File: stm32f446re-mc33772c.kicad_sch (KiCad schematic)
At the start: 47 parts, among them J1 Conn_01x02, J2 USB_B_Micro, J3 Conn_01x03, J4 Conn_01x03, J6 SM06B-GHS-TB, U1 STM32F446RET6, U3 LD1086D2M33TR, U4 AMS1117-3.3, U6 LMR51450SDRRR, U7 SN65HVD232, Y1 16MHz

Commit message: fix: VCAP_1 4.7uF, In1.Cu fill GND
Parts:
- added C62: 4.7u, Capacitor_SMD:C_0402_1005Metric, symbol Device:C
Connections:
- net GND: now also C62.2
- net at U1.30 (VCAP_1): now also C62.1
- no-connect marks 39 -> 38

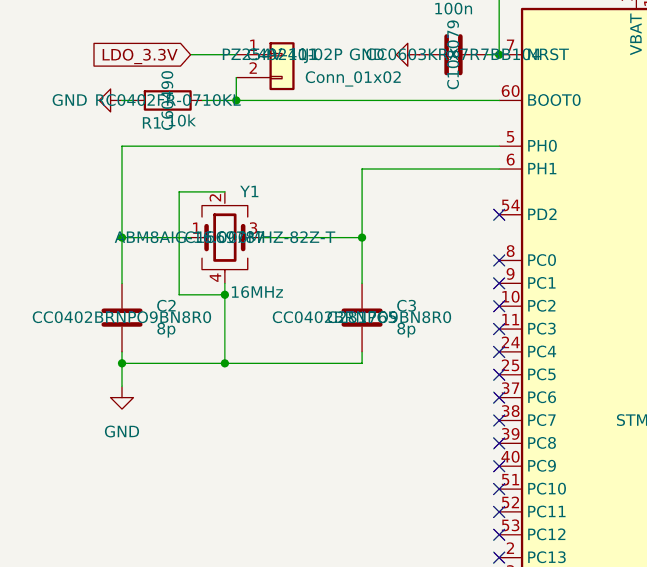
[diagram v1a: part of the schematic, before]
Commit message: change crystal from 16MHz to 8MHz
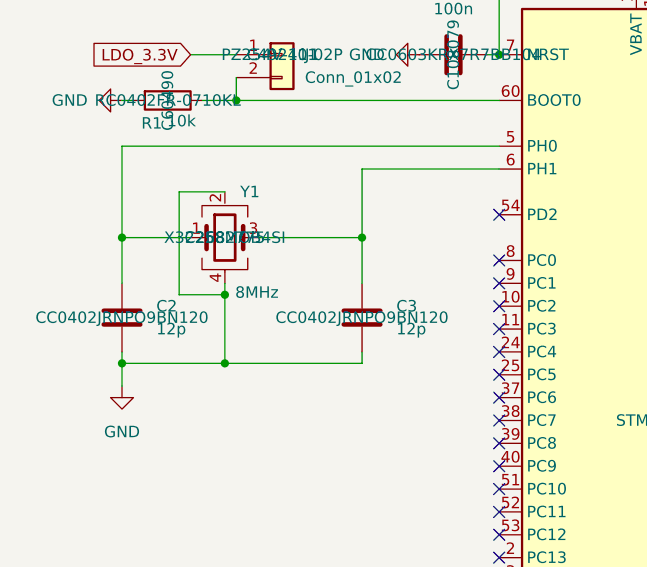
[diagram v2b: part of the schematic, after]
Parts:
- C2, C3: value 8p -> 12p; LCSC Part # C281765 -> C106201; MPN CC0402BRNPO9BN8R0 -> CC0402JRNPO9BN120
- Y1: value 16MHz -> 8MHz; footprint Crystal:Crystal_SMD_Abracon_ABM8AIG-4Pin_3.2x2.5mm -> Crystal:Crystal_SMD_3225-4Pin_3.2x2.5mm; LCSC Part # C1669787 -> C2682775; MPN ABM8AIG-16.000MHZ-82Z-T -> X32258MOB4SI

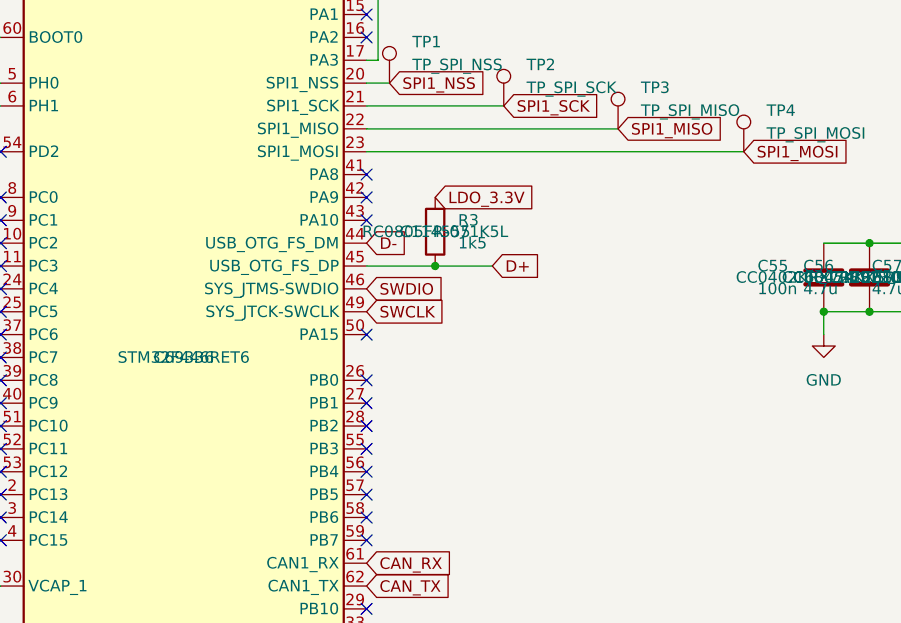
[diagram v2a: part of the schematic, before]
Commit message: add USB OTG FS VBUS sensing
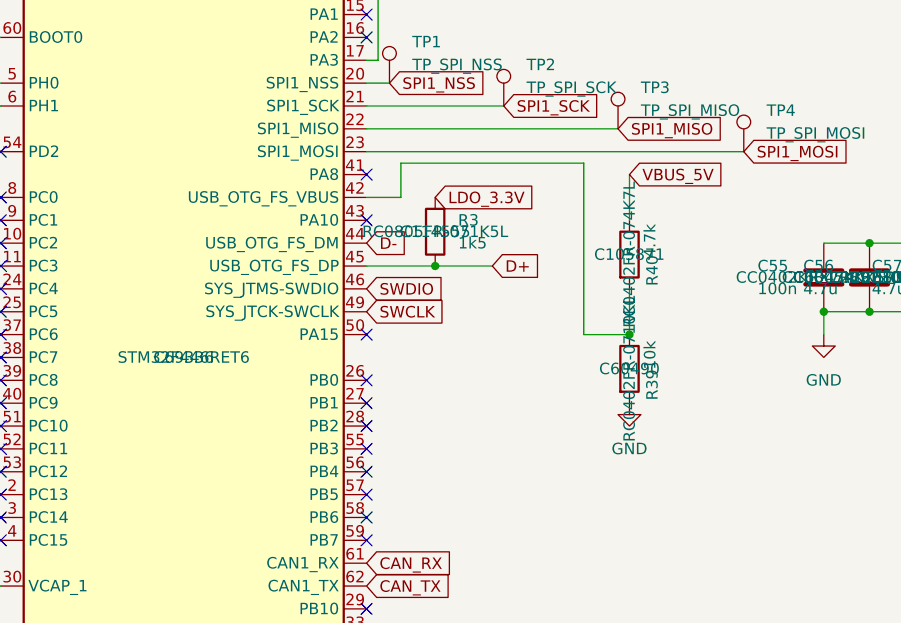
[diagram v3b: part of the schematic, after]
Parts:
- added R39: 10k, Resistor_SMD:R_0402_1005Metric, symbol Device:R
- added R40: 4.7k, Resistor_SMD:R_0402_1005Metric, symbol Device:R
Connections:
- net GND: now also R39.2
- net VBUS_5V: now also R40.1
- net at U1.42 (PA9): now also R39.1, R40.2
- no-connect marks 38 -> 37

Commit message: cleanup sch
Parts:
- removed R3: 1k5, Resistor_SMD:R_0805_2012Metric, symbol Device:R
- removed TP1: TP_SPI_NSS, TestPoint:TestPoint_Pad_D1.0mm, symbol Connector:TestPoint
- removed TP2: TP_SPI_SCK, TestPoint:TestPoint_Pad_D1.0mm, symbol Connector:TestPoint
- removed TP3: TP_SPI_MISO, TestPoint:TestPoint_Pad_D1.0mm, symbol Connector:TestPoint
- removed TP4: TP_SPI_MOSI, TestPoint:TestPoint_Pad_D1.0mm, symbol Connector:TestPoint

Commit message: shrink, SWD
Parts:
- added R3: 10k, Resistor_SMD:R_0402_1005Metric, symbol Device:R
- J3: value Conn_01x03 -> Conn_01x04; footprint Connector_PinHeader_2.54mm:PinHeader_1x03_P2.54mm_Vertical -> Connector_PinHeader_2.54mm:PinHeader_1x04_P2.54mm_Vertical; symbol Connector_Generic:Conn_01x03 -> Connector_Generic:Conn_01x04; FT Rotation Offset 90 -> (none); LCSC Part # C2937625 -> (none); MPN PZ254V-11-03P -> (none)
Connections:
- net GND: now also C10.1, C11.1, C6.1, C7.1, C8.1, C9.1, J3.2 (Pin_2); no longer C10.2, C11.2, C6.2, C7.2, C8.2, C9.2, J3.1 (Pin_1)
- net LDO_3V3: now also C10.2, C11.2, C6.2, C7.2, C8.2, C9.2, R3.1; no longer C10.1, C11.1, C6.1, C7.1, C8.1, C9.1
- net SWDIO: now also J3.4 (Pin_4); no longer J3.2 (Pin_2)
- net nRST: now also J3.1 (Pin_1), R3.2
- net VDDA_3.3V: no longer names the net of C12.1, C13.1, R2.1, U1.13 (VDDA)
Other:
- moved on the sheet: C6, C7
